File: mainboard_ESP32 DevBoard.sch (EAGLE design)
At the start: 37 parts, among them IC1 LM358N, IC2 LM833N, IC3 74HC08N, K1 AQH213, X1 JST-XH-02-PIN-LONG-PAD, X2 JST-XH-04-PIN-LONG-PAD, X3 1751248, X4 1751248

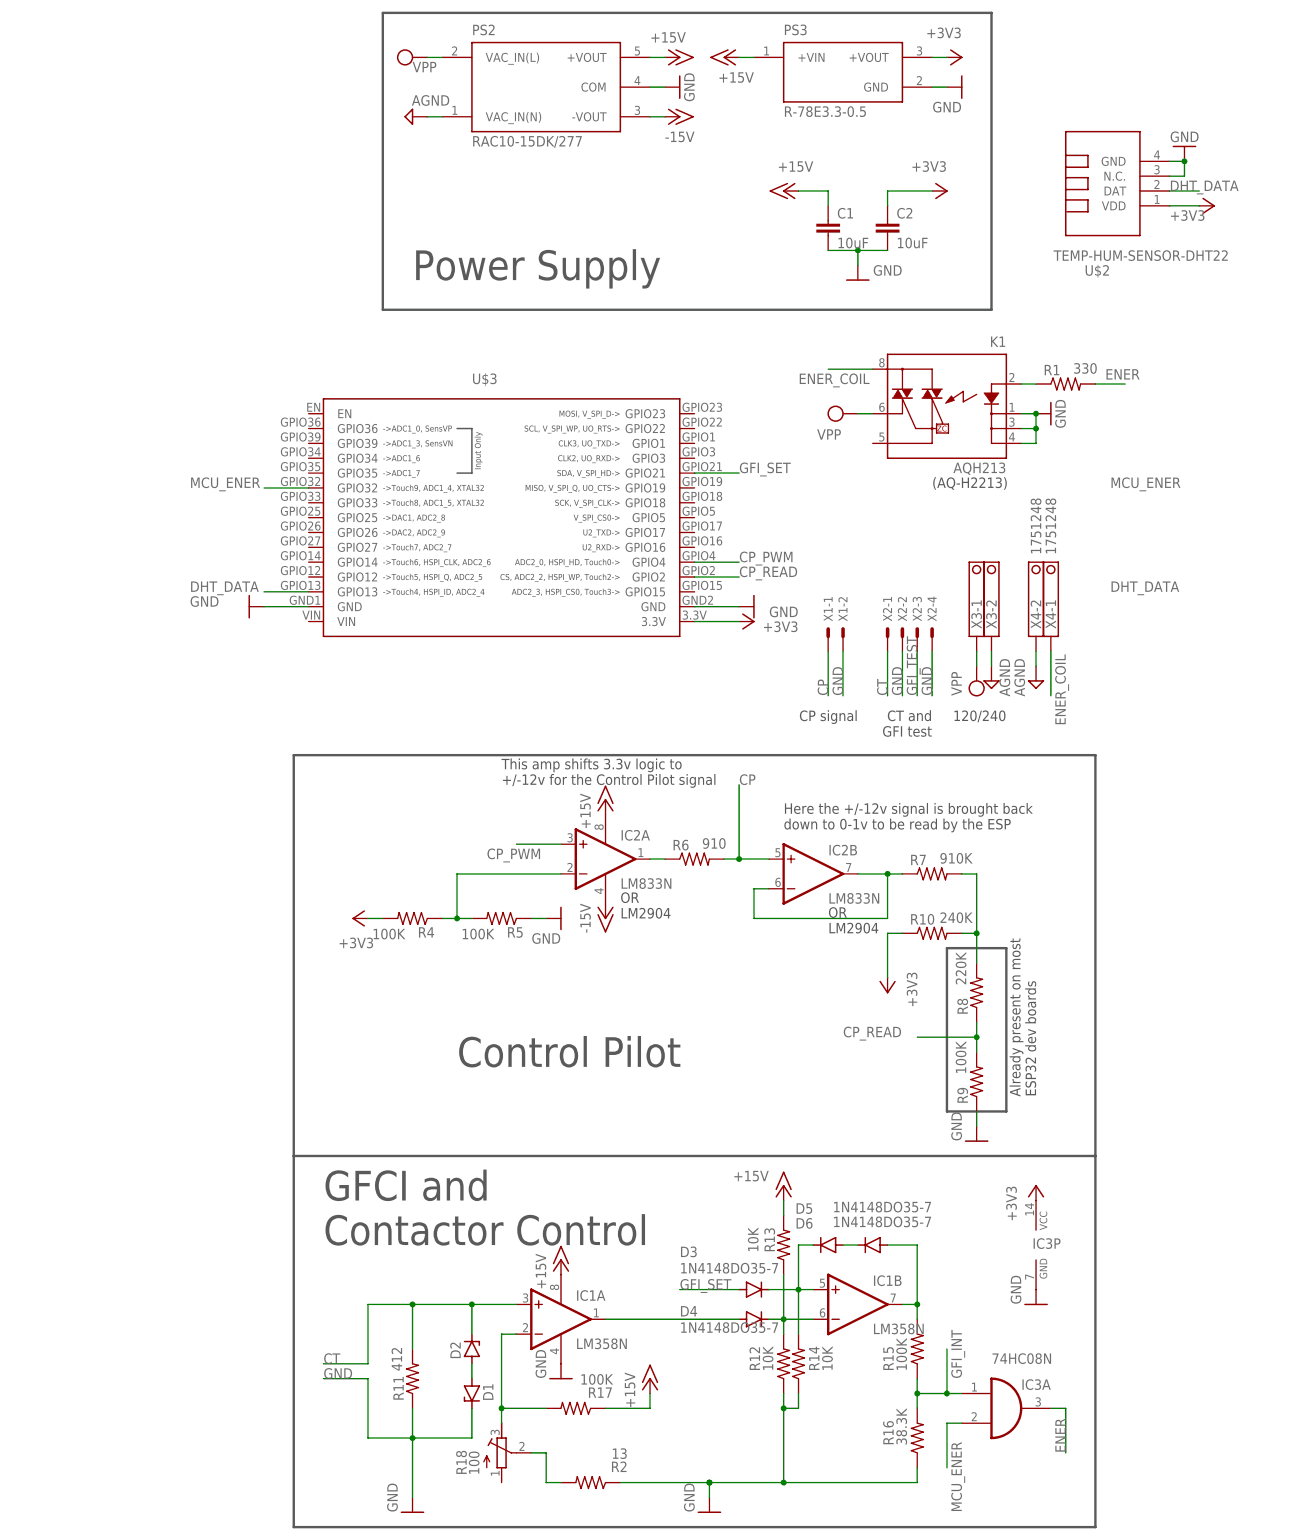
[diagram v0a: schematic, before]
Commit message: Completed routing first try of board. Some pin changes to fit the board better. Added puldown and jumper to prevent accidental coil energize.
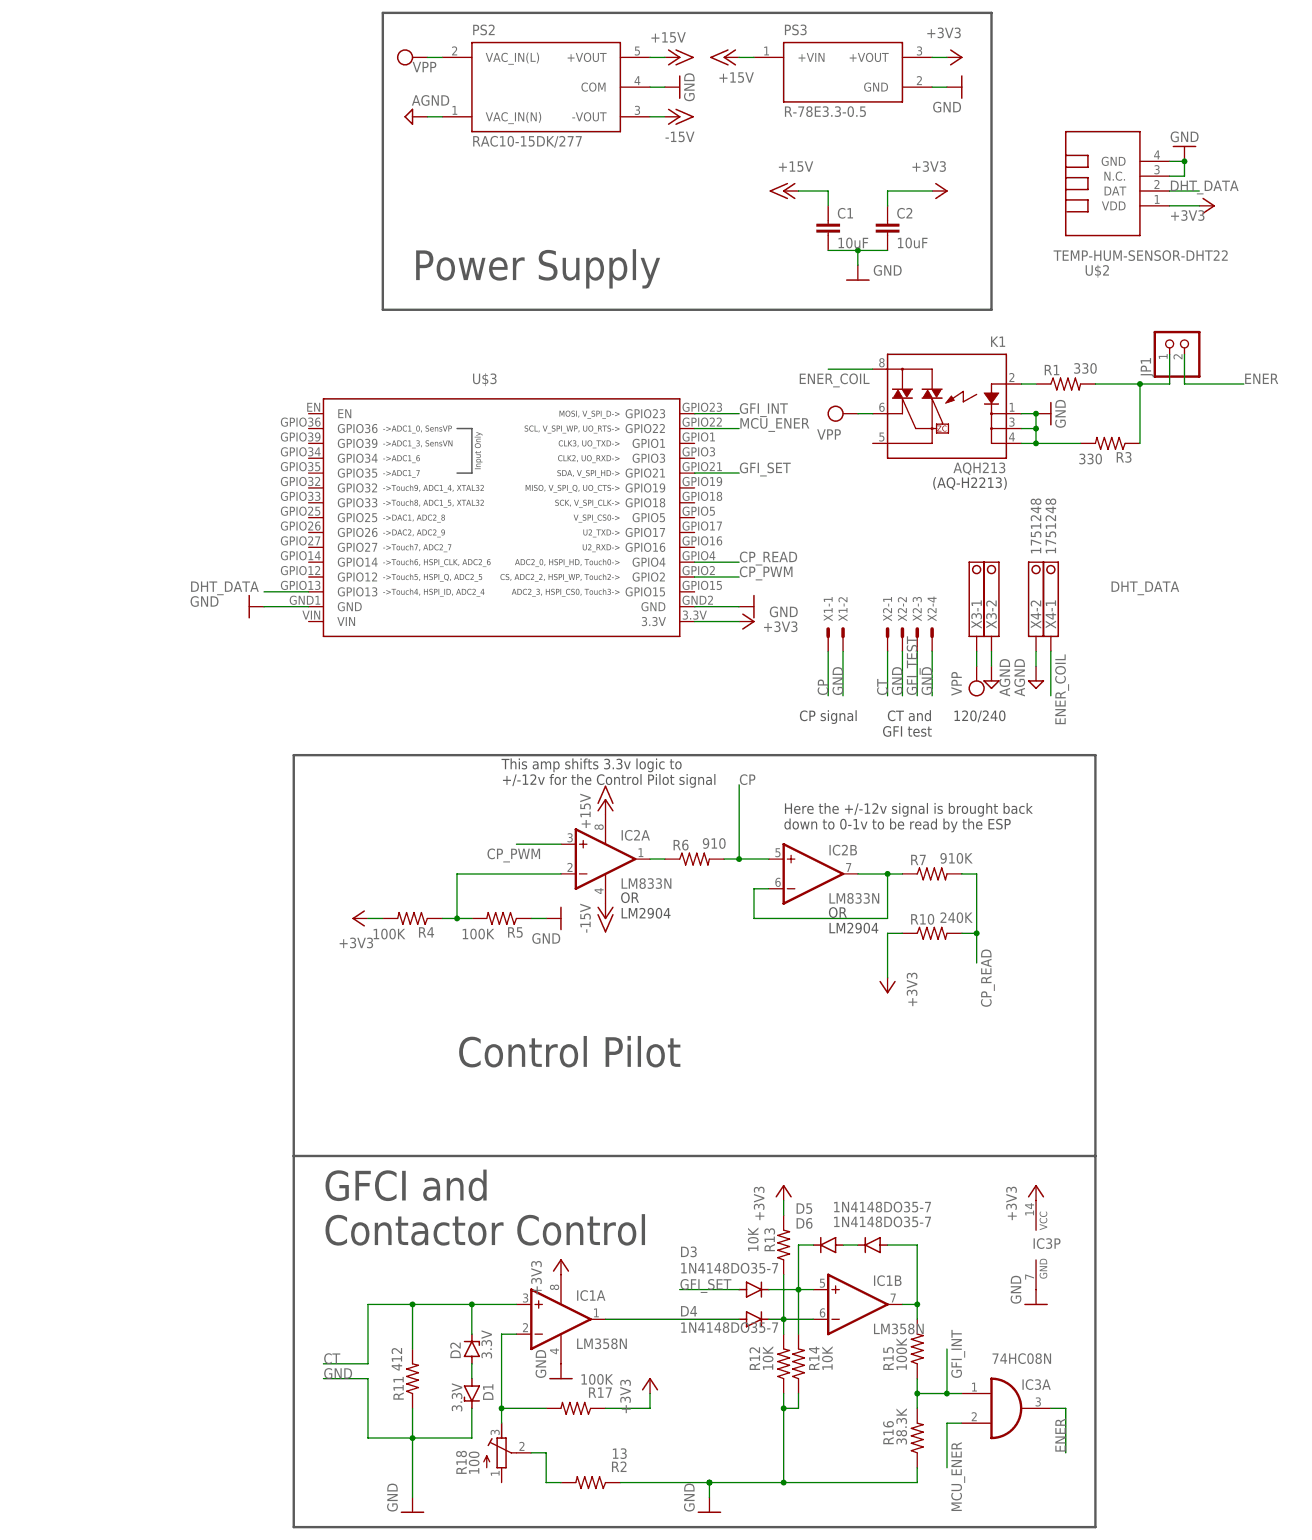
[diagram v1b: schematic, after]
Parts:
- removed R8: 220K, rcl:R-US_0204/7
- removed R9: 100K, rcl:R-US_0204/7
- added JP1: (no value), pinhead:PINHD-1X2
- added R3: 330, rcl:R-US_0204/7
- D1, D2: value (none) -> 3.3V
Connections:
- removed net N$18: R10.2, R7.2, R8.2
- new net N$3: JP1.1, R1.2, R3.1
- net +15V: no longer IC1P.V+, R13.2, R17.1
- net +3V3: now also IC1P.V+, R13.2, R17.1
- net CP_PWM: now also U$3.GPIO2; no longer U$3.GPIO4
- net CP_READ: now also R10.2, R7.2, U$3.GPIO4; no longer R8.1, R9.2, U$3.GPIO2
- net ENER: now also JP1.2; no longer R1.2
- net GFI_INT: now also U$3.GPIO23
- net GND: now also R3.2; no longer R9.1
- net MCU_ENER: now also U$3.GPIO22; no longer U$3.GPIO32
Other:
- note removed: "Already present on most ESP32 dev boards"

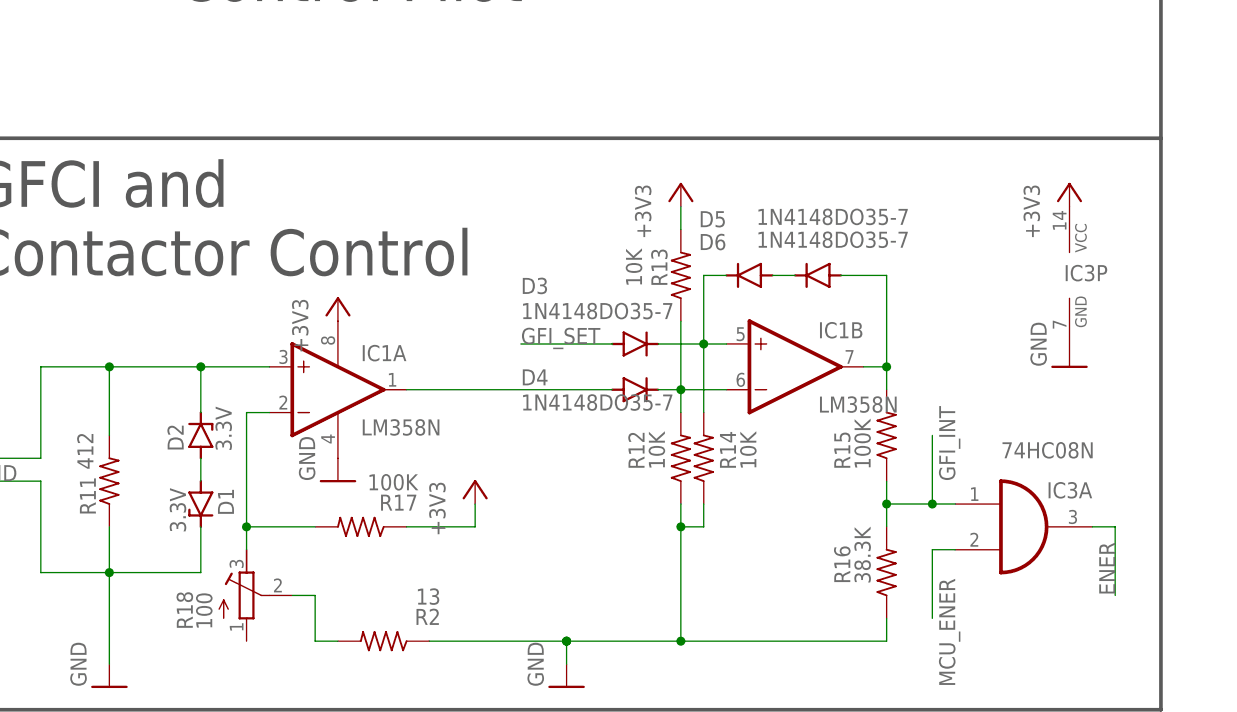
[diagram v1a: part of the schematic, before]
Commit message: Tweaked resistor on GFI circuit to allow 3.3v logic to set the latch
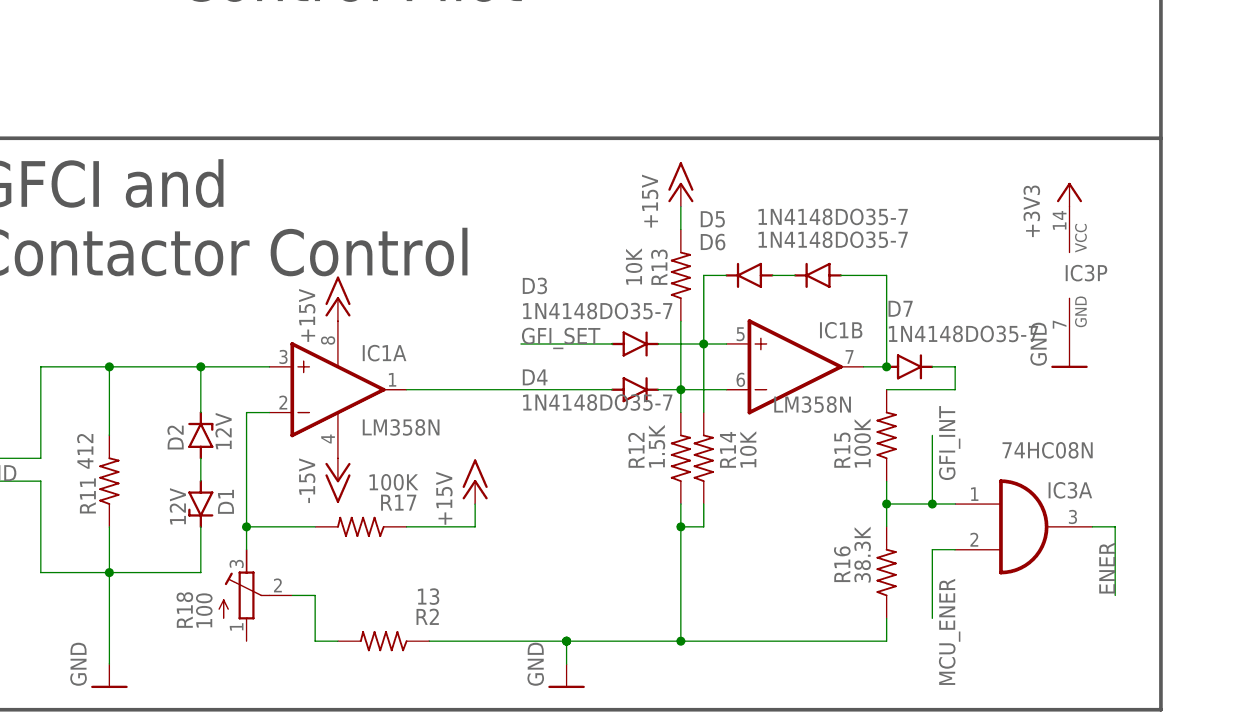
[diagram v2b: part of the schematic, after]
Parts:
- added D7: 1N4148DO35-7, diode:1N4148DO35-7
- D1, D2: value 3.3V -> 12V
- R12: value 10K -> 1.5K
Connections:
- removed net N$11: D6.A, IC1B.OUT, R15.2
- new net N$4: D6.A, D7.A, IC1B.OUT
- new net N$7: D7.C, R15.2
- net +15V: now also IC1P.V+, R13.2, R17.1
- net +3V3: no longer IC1P.V+, R13.2, R17.1
- net -15V: now also IC1P.V-
- net GND: no longer IC1P.V-
